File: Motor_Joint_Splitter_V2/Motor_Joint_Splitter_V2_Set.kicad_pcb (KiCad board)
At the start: 2 copper layers, 45 x 45 mm, 21 parts, among them J2 26605030, J7 ethernet_54602-908LF, J8 motor_connector_292206-8, J9 Conn_01x05, U2 74ACT244MTCX

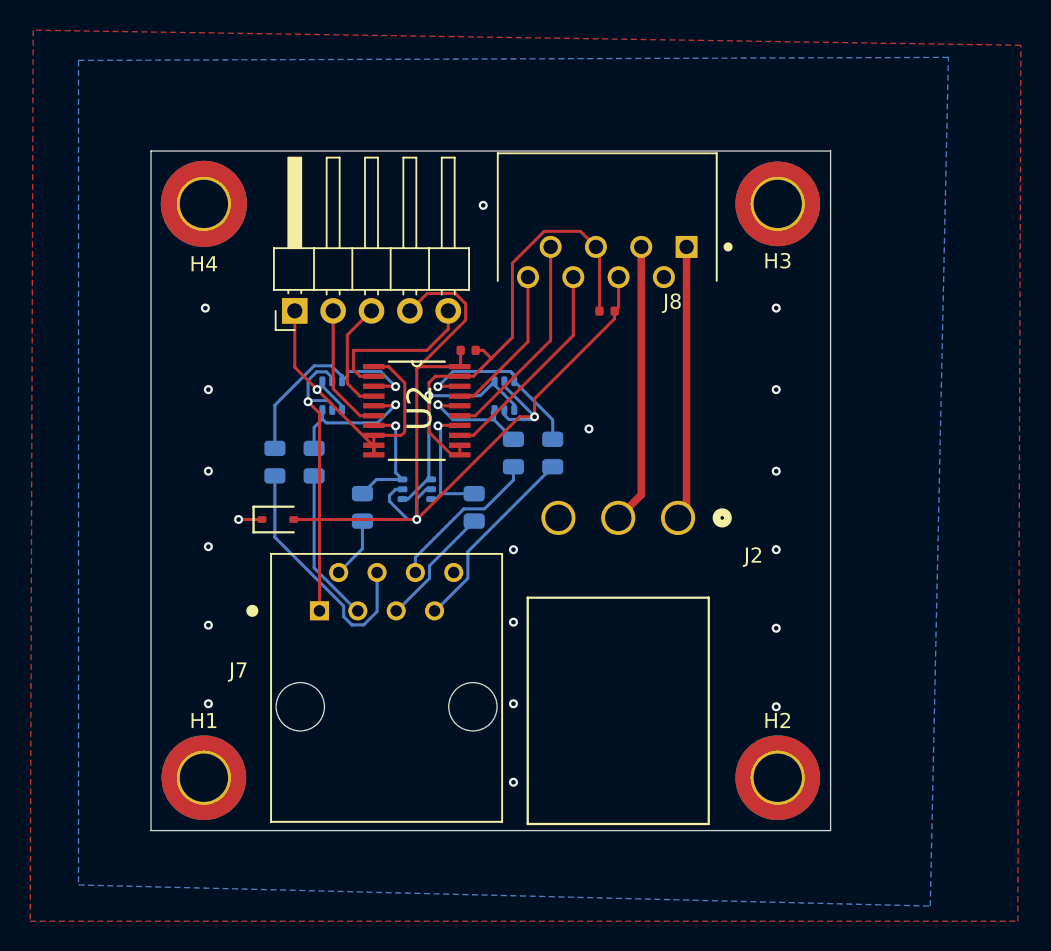
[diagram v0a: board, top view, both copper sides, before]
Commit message: Finalized board, order for it is sitting on JLCPCB's website and everything looks good.
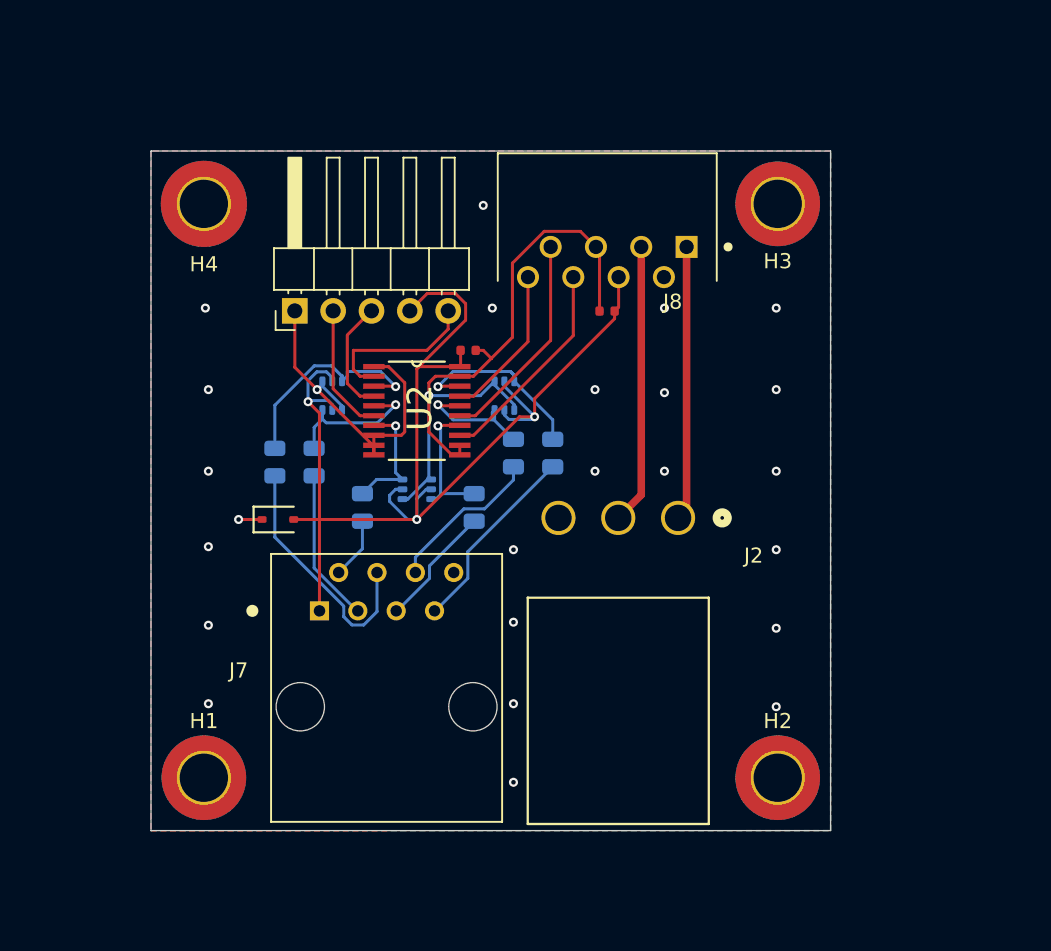
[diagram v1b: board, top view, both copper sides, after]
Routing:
- net GND: vias 21 -> 26
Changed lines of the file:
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@@
+	)
+	(via
+		(at 214 70.4)
+		(size 0.6)
+		(drill 0.3)
+		(layers "F.Cu" "B.Cu")
+		(free yes)
+		(net 1)
 	)
 	(via
@@
 	)
 	(via
+		(at 209.4 81.2)
+		(size 0.6)
+		(drill 0.3)
+		(layers "F.Cu" "B.Cu")
+		(free yes)
+		(net 1)
+	)
+	(via
 		(at 191 75.8)
 		(size 0.6)
@@
 	)
 	(via
-		(at 209 78.4)
-		(size 0.6)
-		(drill 0.3)
-		(layers "F.Cu" "B.Cu")
-		(free yes)
-		(net 1)
-	)
-	(via
 		(at 198.4 76.2)
 		(size 0.6)
@@
 	)
 	(via
+		(at 202.6 70.4)
+		(size 0.6)
+		(drill 0.3)
+		(layers "F.Cu" "B.Cu")
+		(free yes)
+		(net 1)
+	)
+	(via
+		(at 214 81.2)
+		(size 0.6)
+		(drill 0.3)
+		(layers "F.Cu" "B.Cu")
+		(free yes)
+		(net 1)
+	)
+	(via
 		(at 221.4 81.2)
 		(size 0.6)
@@
 	(via
 		(at 183.8 96.6)
+		(size 0.6)
+		(drill 0.3)
+		(layers "F.Cu" "B.Cu")
+		(free yes)
+		(net 1)
+	)
+	(via
+		(at 209.4 75.8)
+		(size 0.6)
+		(drill 0.3)
+		(layers "F.Cu" "B.Cu")
+		(free yes)
+		(net 1)
+	)
+	(via
+		(at 214 76)
 		(size 0.6)
 		(drill 0.3)
@@
 		(priority 1)
 		(connect_pads
-			(clearance 2)
+			(clearance 0.6)
 		)
 		(min_thickness 0.25)
@@
 		(polygon
 			(pts
-				(xy 237.4 111) (xy 237.6 53) (xy 172.2 52) (xy 172 111)
+				(xy 225 105) (xy 225 60) (xy 180 60) (xy 179.982987 105.017013)
 			)
 		)
@@
 		(polygon
 			(pts
-				(xy 231.6 110) (xy 232.8 53.8) (xy 175.2 54) (xy 175.2 108.6)
+				(xy 225 105) (xy 225 60) (xy 180 60.004975) (xy 179.982579 105.017421)
 			)
 		)
